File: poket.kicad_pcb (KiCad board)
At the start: 2 copper layers, 0 parts

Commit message: PCB placement + parametric FreeCAD enclosure
80x54mm 4-layer board, all 90 footprints placed, GND pours on all four
layers with an antenna notch. Enclosure built headless in FreeCAD:
two shells plus slider cap, STEP + STL exported.
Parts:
- added C1: 10uF, Capacitor_SMD:C_0805_2012Metric, F.Cu at (19.5, 24.0)
- added C10: 100nF, Capacitor_SMD:C_0603_1608Metric, F.Cu at (51.0, 16.0)
- added C11: 1uF, Capacitor_SMD:C_0603_1608Metric, F.Cu at (51.0, 19.5)
- added C12: 100nF, Capacitor_SMD:C_0603_1608Metric, F.Cu at (25.5, 28.0)
- added C13: 10uF, Capacitor_SMD:C_0805_2012Metric, F.Cu at (29.5, 28.0)
- added C14: 100nF, Capacitor_SMD:C_0603_1608Metric, F.Cu at (22.0, 9.00)
- added C15: 100nF, Capacitor_SMD:C_0603_1608Metric, F.Cu at (22.0, 12.5)
- added C16: 10uF, Capacitor_SMD:C_0805_2012Metric, F.Cu at (22.0, 16.5)
- added C17: 2.2uF, Capacitor_SMD:C_0603_1608Metric, F.Cu at (33.0, 9.00)
- added C18: 1uF, Capacitor_SMD:C_0603_1608Metric, F.Cu at (33.0, 12.5)
- added C19: 1uF, Capacitor_SMD:C_0603_1608Metric, F.Cu at (33.0, 16.0)
- added C2: 100nF, Capacitor_SMD:C_0603_1608Metric, F.Cu at (19.5, 28.0)
- added C20: 1uF, Capacitor_SMD:C_0603_1608Metric, F.Cu at (36.5, 9.00)
- added C21: 1uF, Capacitor_SMD:C_0603_1608Metric, F.Cu at (36.5, 13.0)
- added C22: 1uF, Capacitor_SMD:C_0603_1608Metric, F.Cu at (43.5, 9.00)
- added C23: 1uF, Capacitor_SMD:C_0603_1608Metric, F.Cu at (43.5, 12.5)
- added C24: 1uF, Capacitor_SMD:C_0603_1608Metric, F.Cu at (43.5, 16.0)
- added C25: 10uF, Capacitor_SMD:C_0805_2012Metric, F.Cu at (47.5, 9.00)
- added C26: 100nF, Capacitor_SMD:C_0603_1608Metric, F.Cu at (47.5, 13.0)
- added C27: 100nF, Capacitor_SMD:C_0603_1608Metric, F.Cu at (40.5, 49.0)
- added C28: 100nF, Capacitor_SMD:C_0603_1608Metric, F.Cu at (75.5, 27.5)
- added C29: 100nF, Capacitor_SMD:C_0603_1608Metric, F.Cu at (75.5, 33.5)
- added C3: 10uF, Capacitor_SMD:C_0805_2012Metric, F.Cu at (4.00, 32.0)
- added C30: 10nF, Capacitor_SMD:C_0603_1608Metric, F.Cu at (44.0, 28.0)
- added C31: 10nF, Capacitor_SMD:C_0603_1608Metric, F.Cu at (26.5, 32.0)
- added C4: 10uF, Capacitor_SMD:C_0805_2012Metric, F.Cu at (4.00, 24.0)
- added C5: 10uF, Capacitor_SMD:C_0805_2012Metric, F.Cu at (12.5, 24.0)
- added C6: 100nF, Capacitor_SMD:C_0603_1608Metric, F.Cu at (16.0, 24.0)
- added C7: 10uF, Capacitor_SMD:C_0805_2012Metric, F.Cu at (33.0, 20.0)
- added C8: 100nF, Capacitor_SMD:C_0603_1608Metric, F.Cu at (38.0, 20.0)
- added C9: 10uF, Capacitor_SMD:C_0805_2012Metric, F.Cu at (51.0, 12.0)
- added D1: WS2812B-2020, LED_SMD:LED_WS2812B-2020_PLCC4_2.0x2.0mm, F.Cu at (44.0, 49.0)
- added D2: CHG, LED_SMD:LED_0603_1608Metric, F.Cu at (47.5, 49.0)
- added D3: B5819W, Diode_SMD:D_SOD-123, F.Cu at (3.50, 28.0)
- added FB1: 600R_100MHz, Inductor_SMD:L_0603_1608Metric, F.Cu at (28.0, 21.0)
- added J1: USB-C, Connector_USB:USB_C_Receptacle_HCTL_HC-TYPE-C-16P-01A, F.Cu at (60.0, 50.3)
- added J2: microSD, Connector_Card:microSD_HC_Hirose_DM3AT-SF-PEJM5, B.Cu at (13.8, 30.0)
- added J3: 3.5mm_TRS, Connector_Audio:Jack_3.5mm_CUI_SJ1-3535NG_Horizontal, F.Cu at (12.0, 5.25)
- added J4: OLED-SSD1306, Connector_PinHeader_2.54mm:PinHeader_1x04_P2.54mm_Vertical, F.Cu at (23.0, 5.50)
- added J5: BATT-JST, Connector_JST:JST_PH_S2B-PH-SM4-TB_1x02-1MP_P2.00mm_Horizontal, F.Cu at (12.0, 49.5)
- added J6: DEBUG-UART, Connector_PinHeader_2.54mm:PinHeader_1x04_P2.54mm_Vertical, F.Cu at (30.0, 36.0)
- added MH1: MountingHole_2.2mm, MountingHole:MountingHole_2.2mm, F.Cu at (5.00, 5.00)
- added MH2: MountingHole_2.2mm, MountingHole:MountingHole_2.2mm, F.Cu at (75.0, 5.00)
- added MH3: MountingHole_2.2mm, MountingHole:MountingHole_2.2mm, F.Cu at (5.00, 48.0)
- added MH4: MountingHole_2.2mm, MountingHole:MountingHole_2.2mm, F.Cu at (75.0, 48.0)
- added Q1: DMG2301L, Package_TO_SOT_SMD:SOT-23, F.Cu at (8.50, 32.0)
- added R1: 5.1k, Resistor_SMD:R_0603_1608Metric, F.Cu at (68.0, 44.0)
- added R10: 4.7k, Resistor_SMD:R_0603_1608Metric, F.Cu at (23.5, 21.0)
- added R11: 10k, Resistor_SMD:R_0603_1608Metric, F.Cu at (26.0, 24.0)
- added R12: 10k, Resistor_SMD:R_0603_1608Metric, F.Cu at (29.5, 24.0)
- added R13: 10k, Resistor_SMD:R_0603_1608Metric, F.Cu at (33.0, 24.0)
- added R14: 10k, Resistor_SMD:R_0603_1608Metric, F.Cu at (36.5, 24.0)
- added R15: 10k, Resistor_SMD:R_0603_1608Metric, F.Cu at (40.0, 24.0)
- added R16: 10k, Resistor_SMD:R_0603_1608Metric, F.Cu at (43.5, 24.0)
- added R17: 10k, Resistor_SMD:R_0603_1608Metric, F.Cu at (28.0, 18.0)
- added R18: 10k, Resistor_SMD:R_0603_1608Metric, F.Cu at (40.0, 17.0)
- added R19: 10k, Resistor_SMD:R_0603_1608Metric, F.Cu at (47.5, 17.0)
- added R2: 5.1k, Resistor_SMD:R_0603_1608Metric, F.Cu at (68.0, 47.0)
- added R20: 100k, Resistor_SMD:R_0603_1608Metric, F.Cu at (47.5, 21.0)
- added R21: 100k, Resistor_SMD:R_0603_1608Metric, F.Cu at (19.5, 32.0)
- added R22: 100k, Resistor_SMD:R_0603_1608Metric, F.Cu at (23.0, 32.0)
- added R23: 1k, Resistor_SMD:R_0603_1608Metric, F.Cu at (75.5, 30.5)
- added R24: 0.01, Resistor_SMD:R_1206_3216Metric, F.Cu at (75.5, 37.0)
- added R25: 10k, Resistor_SMD:R_0603_1608Metric, F.Cu at (33.5, 28.0)
- added R26: 10k, Resistor_SMD:R_0603_1608Metric, F.Cu at (37.0, 28.0)
- added R27: 10k, Resistor_SMD:R_0603_1608Metric, F.Cu at (40.5, 28.0)
- added R28: 10k, Resistor_SMD:R_0603_1608Metric, F.Cu at (30.0, 32.0)
- added R29: 10k, Resistor_SMD:R_0603_1608Metric, F.Cu at (33.5, 32.0)
- added R3: 2k, Resistor_SMD:R_0603_1608Metric, F.Cu at (12.5, 28.0)
- added R30: 10k, Resistor_SMD:R_0603_1608Metric, F.Cu at (37.0, 32.0)
- added R4: 1k, Resistor_SMD:R_0603_1608Metric, F.Cu at (16.0, 28.0)
- added R5: 10k, Resistor_SMD:R_0603_1608Metric, F.Cu at (12.5, 32.0)
- added R6: 1M, Resistor_SMD:R_0603_1608Metric, F.Cu at (16.0, 32.0)
- added R7: 10k, Resistor_SMD:R_0603_1608Metric, F.Cu at (51.0, 23.0)
- added R8: 10k, Resistor_SMD:R_0603_1608Metric, F.Cu at (51.0, 26.5)
- added R9: 4.7k, Resistor_SMD:R_0603_1608Metric, F.Cu at (20.0, 21.0)
- added SW1: EC11E-Switch, Rotary_Encoder:RotaryEncoder_Alps_EC11E-Switch_Vertical_H20mm, F.Cu at (52.0, 33.2)
- added SW2: PREV, Button_Switch_SMD:SW_Push_1TS009xxxx-xxxx-xxxx_6x6x5mm, F.Cu at (24.0, 43.0)
- added SW3: PLAY, Button_Switch_SMD:SW_Push_1TS009xxxx-xxxx-xxxx_6x6x5mm, F.Cu at (33.0, 43.0)
- added SW4: NEXT, Button_Switch_SMD:SW_Push_1TS009xxxx-xxxx-xxxx_6x6x5mm, F.Cu at (42.0, 43.0)
- added SW5: BOOT, Button_Switch_SMD:SW_SPST_B3U-1000P, B.Cu at (32.0, 50.0)
- added SW6: RESET, Button_Switch_SMD:SW_SPST_B3U-1000P, B.Cu at (38.0, 50.0)
- added SW7: PWR, Button_Switch_SMD:SW_SPDT_PCM12, F.Cu at (24.0, 50.5)
- added U1: ESP32-S3-WROOM-1-N16R8, RF_Module:ESP32-S3-WROOM-1, F.Cu at (63.0, 15.0)
- added U2: MCP73831-2-OT, Package_TO_SOT_SMD:SOT-23-5, F.Cu at (8.50, 28.0)
- added U3: AP2112K-3.3, Package_TO_SOT_SMD:SOT-23-5, F.Cu at (8.50, 24.0)
- added U4: PCM5102A, Package_SO:TSSOP-20_4.4x6.5mm_P0.65mm, F.Cu at (28.0, 12.0)
- added U5: PAM8908, Package_DFN_QFN:QFN-16-1EP_3x3mm_P0.5mm_EP1.7x1.7mm, F.Cu at (40.0, 12.0)
- added U6: BQ27441-G1, Package_SON:Texas_S-PDSO-N12, F.Cu at (75.5, 24.0)
- added U7: USBLC6-2SC6, Package_TO_SOT_SMD:SOT-23-6, F.Cu at (52.5, 45.5)
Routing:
- added copper zone on B.Cu, net GND
- added copper zone on F.Cu, net GND
- added copper zone on In1.Cu, net GND
- added copper zone on In2.Cu, net GND
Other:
- board outline added: 80 x 54 mm
- copper layers 2 -> 4

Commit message: Route PCB, 0 DRC errors
Freerouting at 0.2mm track / 0.15mm clearance, GND pours on all four
layers with an antenna notch, 215 stitching vias, silkscreen cleaned up.
DRC: 0 errors, 0 unconnected, 0 schematic parity issues.
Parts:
- moved C28 9.39 mm to (71.5, 36.0)
- moved U6 8.06 mm to (74.5, 32.0)
- moved C29 7.21 mm to (71.5, 39.5)
- moved R23 5.59 mm to (76.5, 36.0)
- moved R24 3.16 mm to (76.5, 40.0)
- moved J5 0.70 mm to (12.0, 48.8)
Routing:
- net 3V3: track 0.00 -> 166.0 mm, vias 0 -> 3
- net VBAT: track 0.00 -> 97.9 mm, vias 0 -> 4
- net VBUS: track 0.00 -> 83.7 mm, vias 0 -> 3
- net I2C_SDA: track 0.00 -> 78.0 mm, vias 0 -> 3
- net ENC_B: track 0.00 -> 74.3 mm, vias 0 -> 2
- net PACK_NEG: track 0.00 -> 74.0 mm, vias 0 -> 2
- net I2C_SCL: track 0.00 -> 72.1 mm, vias 0 -> 2
- net SD_CD: track 0.00 -> 70.1 mm, vias 0 -> 3
- net SD_D1: track 0.00 -> 66.8 mm, vias 0 -> 2
- net SD_D3: track 0.00 -> 64.7 mm, vias 0 -> 2
- net SD_CMD: track 0.00 -> 63.2 mm, vias 0 -> 2
- net SD_D0: track 0.00 -> 62.4 mm, vias 0 -> 3
- net SD_D2: track 0.00 -> 60.8 mm, vias 0 -> 2
- net VBAT_SENSE: track 0.00 -> 60.1 mm, vias 0 -> 2
- net 3V3A: track 0.00 -> 58.5 mm
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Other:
- board text added: "BOOT RST"
- board text added: "POKET"
- board text added: "PWR"
- board text added: "USB-C"
- board text added: "microSD"
- board text added: "rev A"

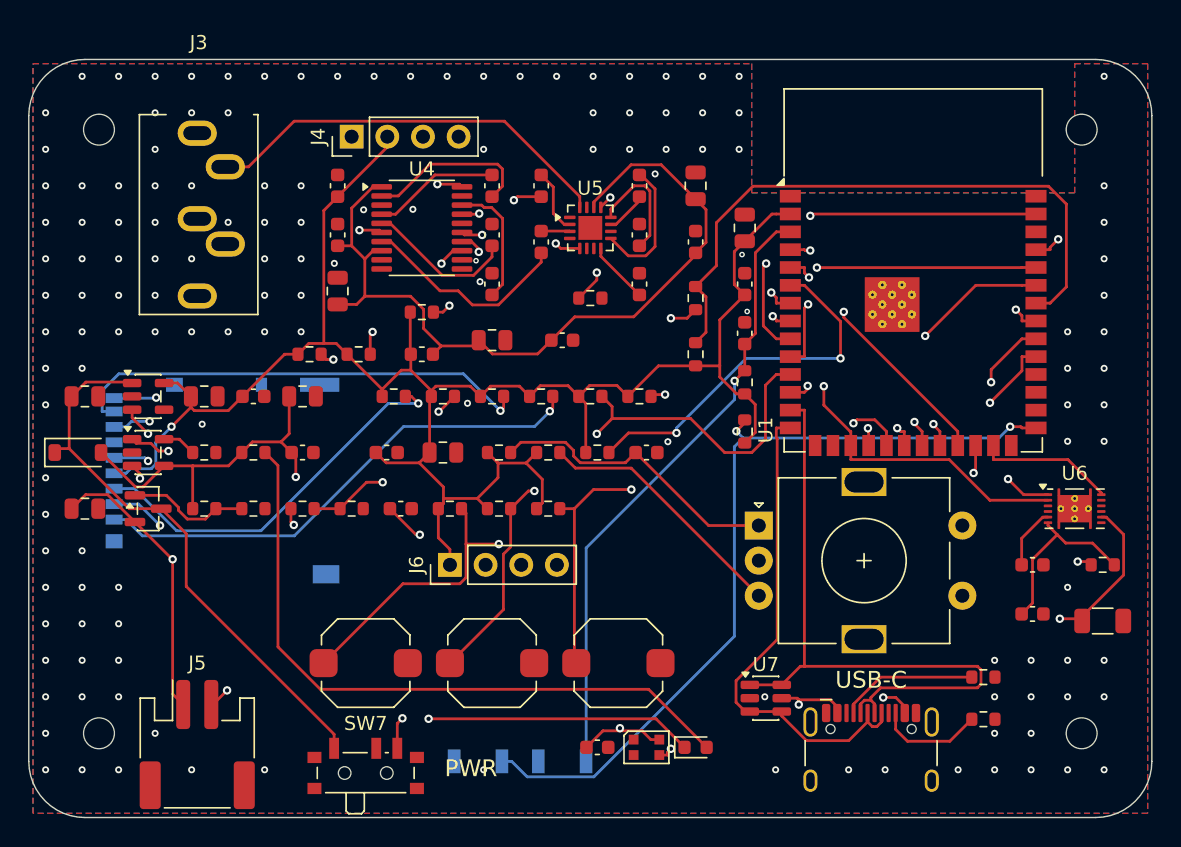
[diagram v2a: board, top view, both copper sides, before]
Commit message: Re-route with In1.Cu as a solid ground plane
Marked In1.Cu as a power layer in the DSN so freerouting leaves it alone;
it now carries no signal copper. Regenerated gerbers, drill, pick-and-place,
BOM and renders. DRC: 0 errors, 0 unconnected, 0 parity.
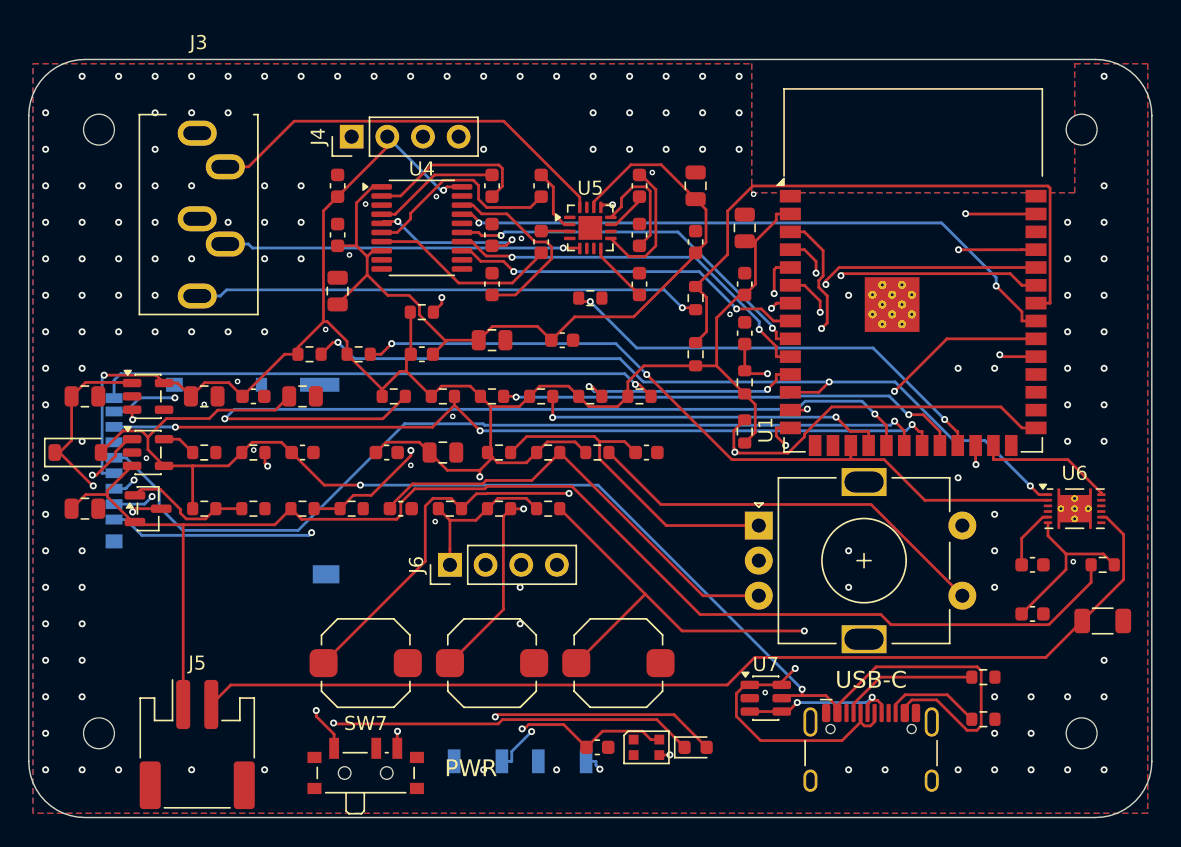
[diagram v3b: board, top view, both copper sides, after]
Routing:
- net VBUS: track 83.7 -> 102.3 mm, vias 3 -> 2
- net ENC_B: track 74.3 -> 58.5 mm, vias 2 -> 1
- net 3V3: track 166.0 -> 177.7 mm, vias 3 -> 4
- net SD_D3: track 64.7 -> 53.7 mm, vias 2 -> 3
- net SD_CMD: track 63.2 -> 73.3 mm, vias 2 -> 3
- net USB_DM: track 48.3 -> 39.4 mm, vias 0 -> 2
- net BTN_NEXT: track 50.5 -> 59.3 mm
- net ESP_EN: track 44.3 -> 53.0 mm, vias 1 -> 3
- net CHG_STAT: track 48.8 -> 55.4 mm
- net LED_DIN: track 32.9 -> 38.7 mm
- net CHG_LED_A: track 47.7 -> 42.1 mm, vias 0 -> 2
- net BTN_PLAY: track 55.8 -> 61.3 mm
- net SD_CLK: track 58.5 -> 63.7 mm, vias 2 -> 1
- net DAC_LDOO: track 9.04 -> 13.8 mm
- net SD_D1: track 66.8 -> 62.2 mm, vias 2 -> 3
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
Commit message: Rev B: swap to ESP32-WROOM-32E-R2 so Bluetooth audio actually works
The ESP32-S3 has Bluetooth LE only - no BR/EDR - so A2DP source, the whole
point of "sends to Bluetooth headphones", could never have worked on it.
ESP-IDF's own soc_caps.h is explicit: esp32 defines SOC_BT_CLASSIC_SUPPORTED,
esp32s3 does not, and CONFIG_BT_CLASSIC_ENABLED is not even a symbol there.

New MCU: ESP32-WROOM-32E-N16R2 (ESP32-D0WDR2-V3, Classic BT + BLE, 16 MB
flash, 2 MB PSRAM in the chip package so GPIO16/17 stay free unlike a WROVER).

Knock-on changes, all verified against datasheets:
- CP2102N-A02-GQFN24 USB-UART bridge; this part has no native USB.
  VBUS sense gets the datasheet's required 22.1k/47.5k divider (abs max on
  that pin is VIO+2.5 V), RSTb a 1k pull-up to VIO, and 4.7uF + 0.1uF at
  every power pin.
- Auto-reset pair wired to Espressif's DevKitC truth table: cross-coupled,
  Q_EN base=DTR emitter=RTS, Q_IO0 base=RTS emitter=DTR, so asserting both
  lines - which opening a serial port does - resets nothing.
- microSD moved from 4-bit SDIO to SPI. The classic ESP32's 4-bit slot puts
  DAT2 on GPIO12/MTDI, the flash-voltage strap; a card's pull-up there tells
  the bootloader the flash is 1.8 V and bricks the boot.
- Battery-sense divider removed: ADC1 is fully consumed by the encoder and
  the input-only buttons, ADC2 dies when Wi-Fi is up, and the BQ27441 already
  reports voltage over I2C.
- GPIO2 strap gets a pull-down; a WS2812 data pin is high-Z.

Firmware: new pin map in board.h, SD over SPI, A2DP compiled in for real
(esp_a2d_source_init is in the binary), plus the app shell, Wi-Fi AP and the
HTTP server that serves the gzipped web UI from rodata.

Schematic ERC 0 errors / 0 warnings; all 20 firmware pins checked against the
netlist export. PCB re-placed and re-routed from scratch: DRC 0 errors, 0
schematic-parity issues, every signal net routed. Three ground-pour fragments
remain untied, two of which carry a bypass cap's ground - documented, not
hidden. Enclosur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
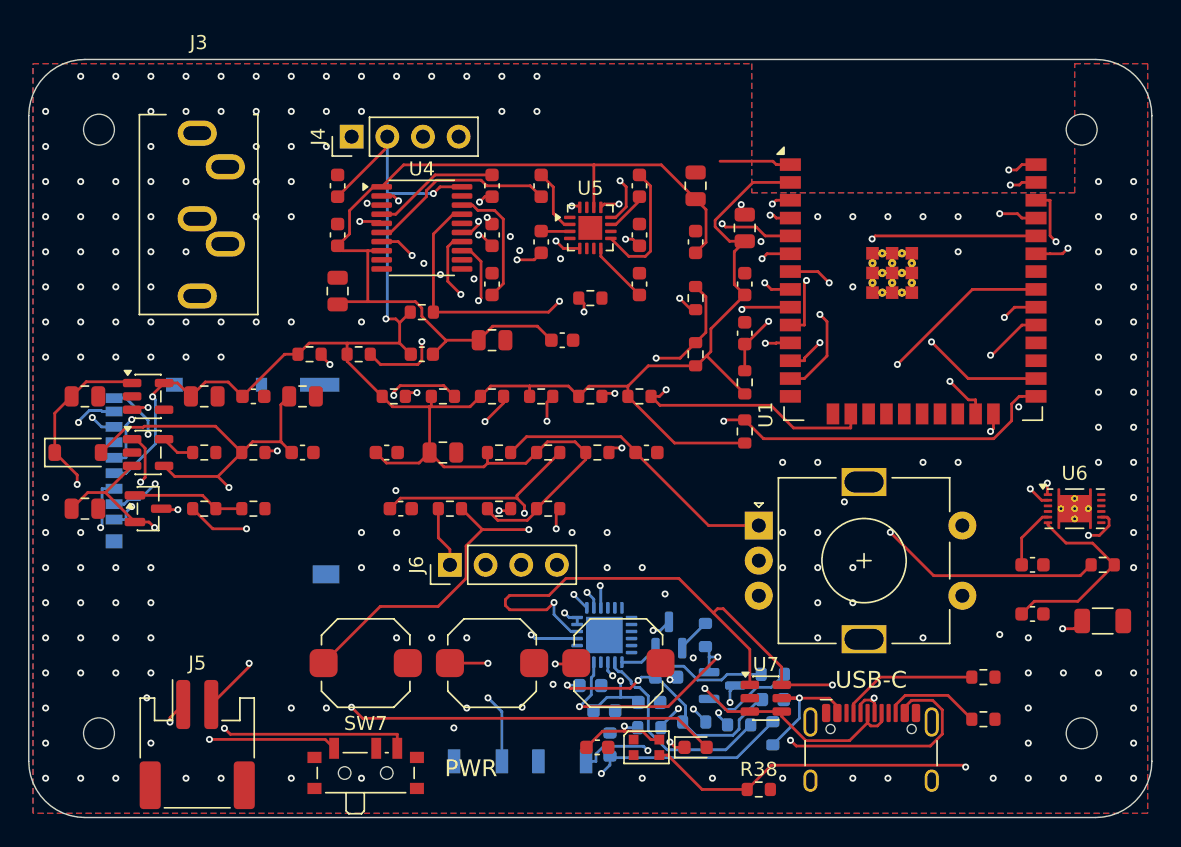
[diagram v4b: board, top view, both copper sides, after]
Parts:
- removed R21, R22: 100k, Resistor_SMD:R_0603_1608Metric
- added C32: 4.7uF, Capacitor_SMD:C_0603_1608Metric, B.Cu at (45.4, 44.0)
- added C33: 100nF, Capacitor_SMD:C_0603_1608Metric, B.Cu at (44.2, 45.8)
- added C34: 100nF, Capacitor_SMD:C_0603_1608Metric, B.Cu at (40.0, 44.6)
- added C35: 4.7uF, Capacitor_SMD:C_0603_1608Metric, B.Cu at (41.0, 46.4)
- added C36: 100nF, Capacitor_SMD:C_0603_1608Metric, B.Cu at (53.0, 45.6)
- added Q2: MMBT3904, Package_TO_SOT_SMD:SOT-23, B.Cu at (45.6, 41.0)
- added Q3: MMBT3904, Package_TO_SOT_SMD:SOT-23, B.Cu at (49.4, 44.6)
- added R31: 1k, Resistor_SMD:R_0603_1608Metric, B.Cu at (47.4, 47.2)
- added R32: 1k, Resistor_SMD:R_0603_1608Metric, B.Cu at (50.6, 47.4)
- added R33: 10k, Resistor_SMD:R_0603_1608Metric, B.Cu at (44.2, 47.6)
- added R34: 22.1k, Resistor_SMD:R_0603_1608Metric, B.Cu at (53.0, 48.0)
- added R35: 47.5k, Resistor_SMD:R_0603_1608Metric, B.Cu at (41.4, 48.8)
- added R36: 10k, Resistor_SMD:R_0603_1608Metric, B.Cu at (48.2, 41.0)
- added R37: 10k, Resistor_SMD:R_0603_1608Metric, B.Cu at (53.0, 43.8)
- added R38: 10k, Resistor_SMD:R_0603_1608Metric, F.Cu at (52.0, 52.0)
- added U8: CP2102N-A02-GQFN24, Package_DFN_QFN:QFN-24-1EP_4x4mm_P0.5mm_EP2.6x2.6mm, B.Cu at (41.0, 41.0)
- U1: value ESP32-S3-WROOM-1-N16R8 -> ESP32-WROOM-32E-N16R2; footprint RF_Module:ESP32-S3-WROOM-1 -> ESP32-WROOM-32E
- moved U1 2.25 mm to (63.0, 12.8)
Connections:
- J2 pad 2: SD_D3 -> SD_CS
- J2 pad 3: SD_CMD -> SD_MOSI
- J2 pad 5: SD_CLK -> SD_SCK
- J2 pad 7: SD_D0 -> SD_MISO
- R11 pad 2: SD_CMD -> SD_MOSI
- R12 pad 2: SD_D0 -> SD_MISO
- R15 pad 2: SD_D3 -> SD_CS
- U1 pad 10: I2S_DIN -> I2S_LRCK
- U1 pad 11: SD_D3 -> I2S_BCK
- U1 pad 12: I2C_SDA -> I2S_DIN
- U1 pad 13: USB_DM -> DAC_XSMT
- U1 pad 14: USB_DP -> (no net)
- U1 pad 15: (no net) -> GND
- U1 pad 16: (no net) -> SD_CD
- U1 pad 17: I2C_SCL -> (no net)
- U1 pad 18: SD_D2 -> (no net)
- U1 pad 19: SD_CMD -> (no net)
- U1 pad 20: SD_CLK -> (no net)
- U1 pad 21: SD_D0 -> (no net)
- U1 pad 22: SD_D1 -> (no net)
- U1 pad 23: AMP_EN -> JACK_DET
- U1 pad 25: FG_GPOUT -> ESP_IO0
- U1 pad 26: (no net) -> AMP_EN
- U1 pad 27: ESP_IO0 -> (no net)
- U1 pad 29: (no net) -> SD_CS
- U1 pad 30: (no net) -> SD_SCK
- U1 pad 31: BTN_PLAY -> SD_MISO
- U1 pad 32: BTN_NEXT -> (no net)
- U1 pad 33: DAC_XSMT -> I2C_SDA
- U1 pad 34: JACK_DET -> UART_RX
- U1 pad 35: SD_CD -> UART_TX
- U1 pad 36: UART_RX -> I2C_SCL
- U1 pad 37: UART_TX -> SD_MOSI
- U1 pad 38: (no net) -> GND
- U1 pad 39: VBAT_SENSE -> GND
- U1 pad 4: ENC_A -> BTN_PLAY
- U1 pad 5: ENC_B -> BTN_NEXT
- U1 pad 6: ENC_SW -> BTN_PREV
- U1 pad 7: BTN_PREV -> ENC_SW
- U1 pad 8: I2S_BCK -> ENC_A
- U1 pad 9: I2S_LRCK -> ENC_B
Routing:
- net SD_MOSI: track 0.00 -> 99.1 mm, vias 0 -> 5
- net SD_MISO: track 0.00 -> 78.4 mm, vias 0 -> 3
- net SD_CMD: track 73.3 -> 0.00 mm, vias 3 -> 0
- net SD_CS: track 0.00 -> 72.2 mm, vias 0 -> 3
- net SD_SCK: track 0.00 -> 71.5 mm, vias 0 -> 2
- net SD_CLK: track 63.7 -> 0.00 mm, vias 1 -> 0
- net SD_D0: track 61.0 -> 0.00 mm, vias 3 -> 0
- net VBAT_SENSE: track 60.4 -> 0.00 mm, vias 2 -> 0
- net SD_D3: track 53.7 -> 0.00 mm, vias 3 -> 0
- net UART_RX: track 47.0 -> 90.0 mm, vias 1 -> 6
- net UART_TX: track 50.5 -> 82.5 mm, vias 1 -> 4
- net 3V3: track 177.7 -> 208.5 mm, vias 4 -> 5
- net CP_VBSENSE: track 0.00 -> 28.8 mm, vias 0 -> 2
- net CP_VDD: track 0.00 -> 27.3 mm, vias 0 -> 4
- net SD_D1: track 62.2 -> 35.4 mm, vias 3 -> 2
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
